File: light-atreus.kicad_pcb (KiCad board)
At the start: 2 copper layers, 40.1 x 44.5 mm, 0 parts

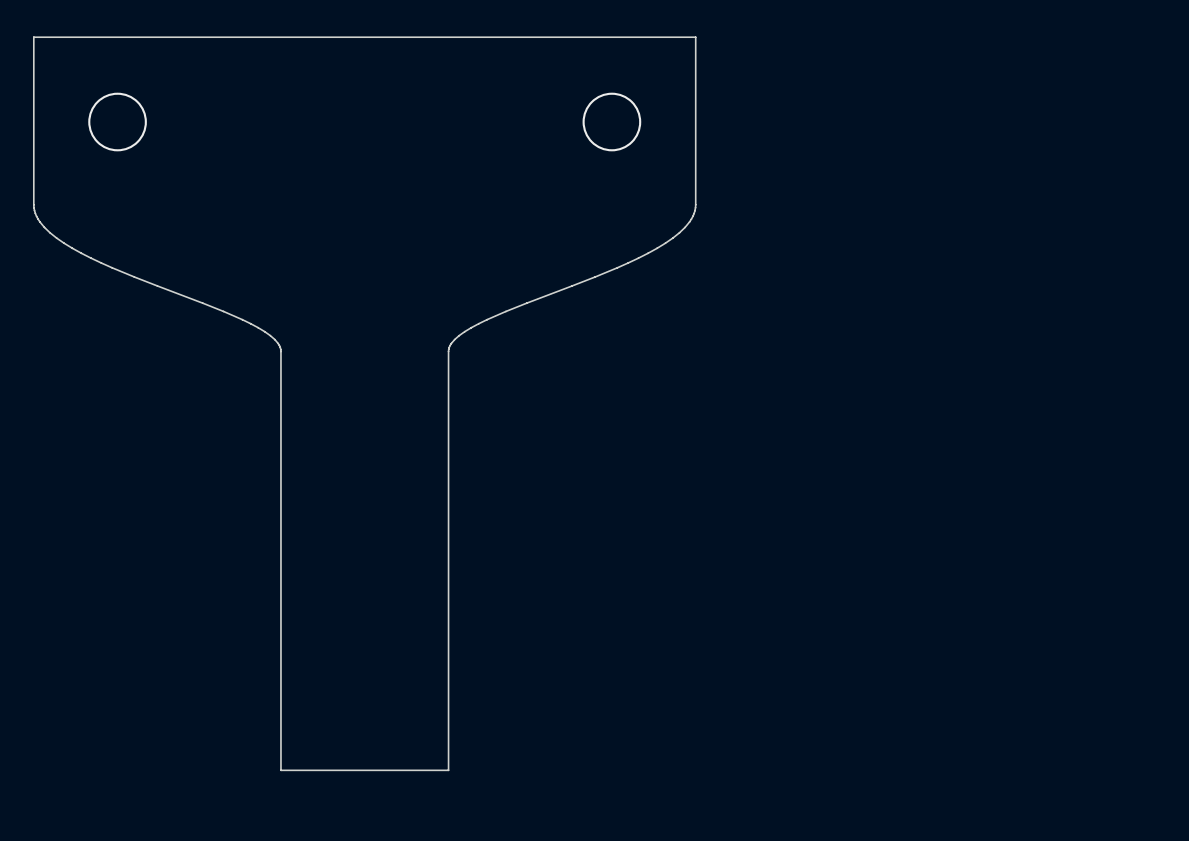
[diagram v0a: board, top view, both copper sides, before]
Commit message: Place USB pads exactly
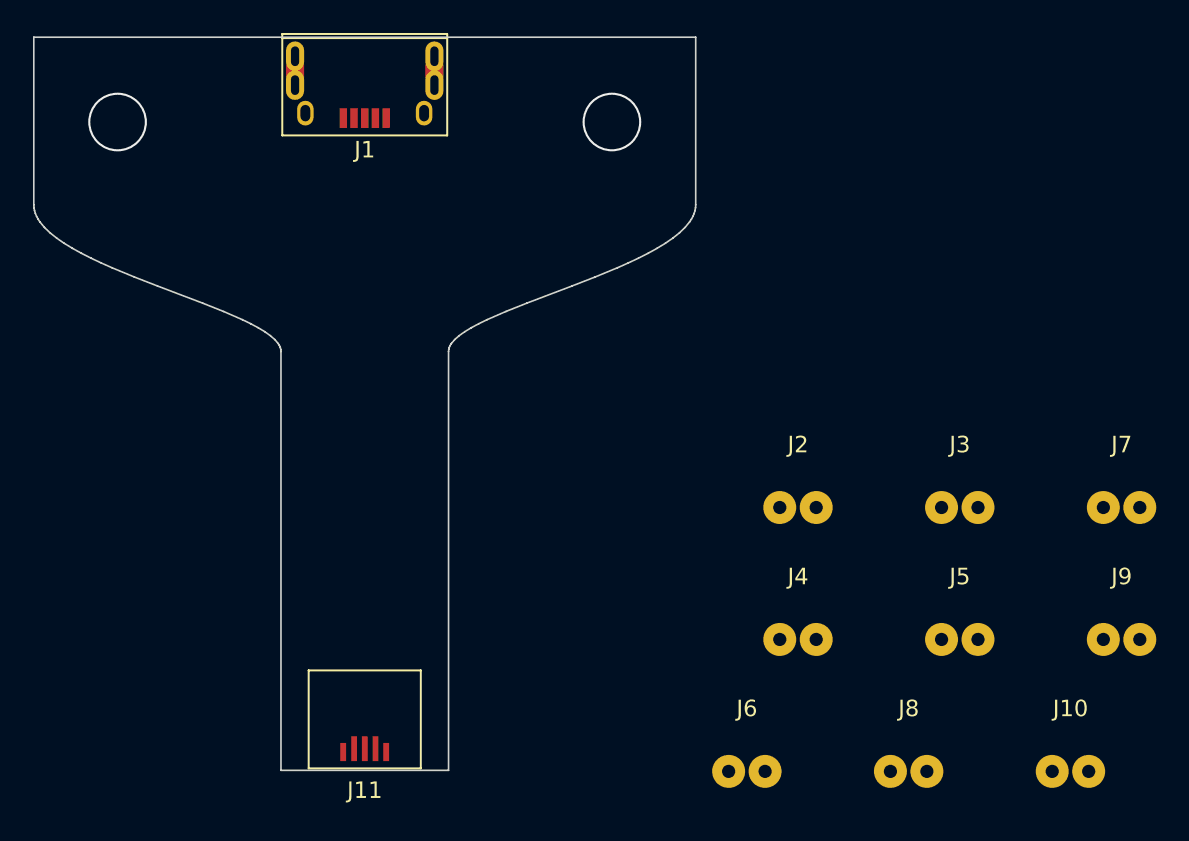
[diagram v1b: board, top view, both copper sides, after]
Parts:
- added J1: USB_B, custom_footprints:USB_Micro-B-custom, F.Cu at (130.3, 75.2)
- added J10: CONN_01X02, custom_footprints:SolderWirePad_1x2-8mm, F.Cu at (173.1, 115.4)
- added J11: USB_B, custom_footprints:USB_Micro-B-custom-plug, F.Cu at (130.3, 114.0)
- added J2: CONN_01X02, custom_footprints:SolderWirePad_1x2-8mm, F.Cu at (156.6, 99.4)
- added J3: CONN_01X02, custom_footprints:SolderWirePad_1x2-8mm, F.Cu at (166.4, 99.4)
- added J4: CONN_01X02, custom_footprints:SolderWirePad_1x2-8mm, F.Cu at (156.6, 107.4)
- added J5: CONN_01X02, custom_footprints:SolderWirePad_1x2-8mm, F.Cu at (166.4, 107.4)
- added J6: CONN_01X02, custom_footprints:SolderWirePad_1x2-8mm, F.Cu at (153.5, 115.4)
- added J7: CONN_01X02, custom_footprints:SolderWirePad_1x2-8mm, F.Cu at (176.2, 99.4)
- added J8: CONN_01X02, custom_footprints:SolderWirePad_1x2-8mm, F.Cu at (163.3, 115.4)
- added J9: CONN_01X02, custom_footprints:SolderWirePad_1x2-8mm, F.Cu at (176.2, 107.4)

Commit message: Locate all wire solder points
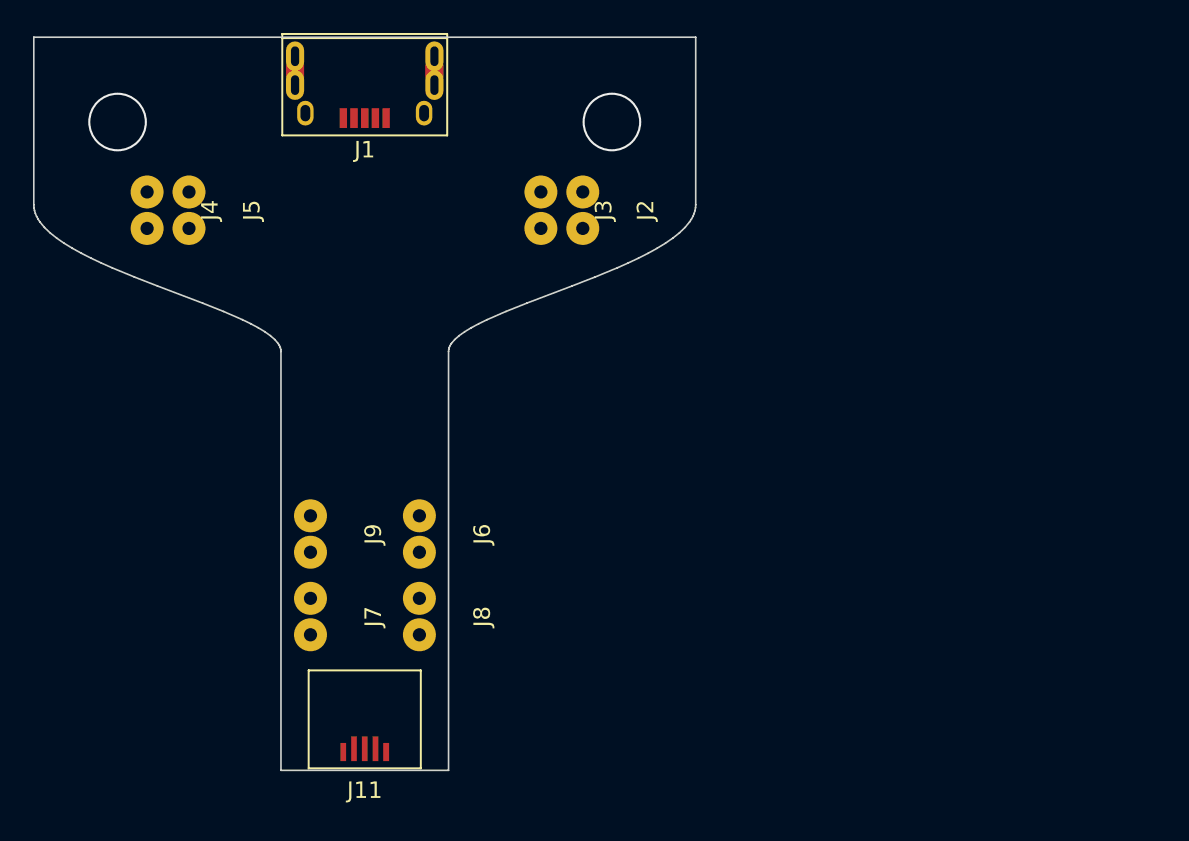
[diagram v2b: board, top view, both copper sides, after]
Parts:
- removed J10: CONN_01X02, custom_footprints:SolderWirePad_1x2-8mm
- moved J5 53.5 mm to (119.6, 81.4), turned to 270 degrees
- moved J7 49.6 mm to (127.0, 106.0), turned to 270 degrees
- moved J9 49.6 mm to (127.0, 101.0), turned to 270 degrees
- moved J4 47.3 mm to (117.1, 81.4), turned to 270 degrees
- moved J3 31.1 mm to (141.0, 81.4), turned to 270 degrees
- moved J8 31.1 mm to (133.6, 106.0), turned to 270 degrees
- moved J6 24.5 mm to (133.6, 101.0), turned to 270 degrees
- moved J2 22.3 mm to (143.5, 81.4), turned to 270 degrees
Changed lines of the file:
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@@
     (tracks 2)
     (zones 0)
-    (modules 11)
-    (nets 15)
+    (modules 10)
+    (nets 14)
   )
   (page A4)
@@
   (net 12 "Net-(J8-Pad2)")
   (net 13 "Net-(J9-Pad2)")
-  (net 14 "Net-(J10-Pad2)")
   (net_class Default "This is the default net class."
     (clearance 0)
@@
     (add_net /SHIELD)
     (add_net /VBUS)
-    (add_net "Net-(J10-Pad2)")
     (add_net "Net-(J2-Pad2)")
     (add_net "Net-(J3-Pad2)")
@@
   )
   (module custom_footprints:SolderWirePad_1x2-8mm (layer F.Cu)
-    (at 156.562257 99.394617)
-    (fp_text reference J2 (at 0 -3.81) (layer F.SilkS)
-      (effects (font (size 1 1) (thickness 0.15)))
-    )
-    (fp_text value CONN_01X02 (at 0.635 2.54) (layer F.Fab)
-      (effects (font (size 1 1) (thickness 0.15)))
-    )
-    (pad 2 thru_hole circle (at 1.1 0) (size 1.99898 1.99898) (drill 0.8001) (layers *.Cu *.Mask)
+    (at 143.51 81.374 270)
+    (fp_text reference J2 (at 0 -3.81 270) (layer F.SilkS)
+      (effects (font (size 1 1) (thickness 0.15)))
+    )
+    (fp_text value CONN_01X02 (at 0.635 2.54 270) (layer F.Fab)
+      (effects (font (size 1 1) (thickness 0.15)))
+    )
+    (pad 2 thru_hole circle (at 1.1 0 270) (size 1.99898 1.99898) (drill 0.8001) (layers *.Cu *.Mask)
       (net 6 "Net-(J2-Pad2)"))
-    (pad 1 thru_hole circle (at -1.11 0) (size 1.99898 1.99898) (drill 0.8001) (layers *.Cu *.Mask)
-      (net 5 /VBUS))
-  )
-  (module custom_footprints:SolderWirePad_1x2-8mm (layer F.Cu)
-    (at 166.372257 99.394617)
-    (fp_text reference J3 (at 0 -3.81) (layer F.SilkS)
-      (effects (font (size 1 1) (thickness 0.15)))
-    )
-    (fp_text value CONN_01X02 (at 0.635 2.54) (layer F.Fab)
-      (effects (font (size 1 1) (thickness 0.15)))
-    )
-    (pad 1 thru_hole circle (at -1.11 0) (size 1.99898 1.99898) (drill 0.8001) (layers *.Cu *.Mask)
-      (net 2 /GND))
-    (pad 2 thru_hole circle (at 1.1 0) (size 1.99898 1.99898) (drill 0.8001) (layers *.Cu *.Mask)
+    (pad 1 thru_hole circle (at -1.11 0 270) (size 1.99898 1.99898) (drill 0.8001) (layers *.Cu *.Mask)
+      (net 5 /VBUS))
+  )
+  (module custom_footprints:SolderWirePad_1x2-8mm (layer F.Cu)
+    (at 140.97 81.374 270)
+    (fp_text reference J3 (at 0 -3.81 270) (layer F.SilkS)
+      (effects (font (size 1 1) (thickness 0.15)))
+    )
+    (fp_text value CONN_01X02 (at 0.635 2.54 270) (layer F.Fab)
+      (effects (font (size 1 1) (thickness 0.15)))
+    )
+    (pad 1 thru_hole circle (at -1.11 0 270) (size 1.99898 1.99898) (drill 0.8001) (layers *.Cu *.Mask)
+      (net 2 /GND))
+    (pad 2 thru_hole circle (at 1.1 0 270) (size 1.99898 1.99898) (drill 0.8001) (layers *.Cu *.Mask)
       (net 7 "Net-(J3-Pad2)"))
   )
   (module custom_footprints:SolderWirePad_1x2-8mm (layer F.Cu)
-    (at 156.562257 107.394617)
-    (fp_text reference J4 (at 0 -3.81) (layer F.SilkS)
-      (effects (font (size 1 1) (thickness 0.15)))
-    )
-    (fp_text value CONN_01X02 (at 0.635 2.54) (layer F.Fab)
-      (effects (font (size 1 1) (thickness 0.15)))
-    )
-    (pad 2 thru_hole circle (at 1.1 0) (size 1.99898 1.99898) (drill 0.8001) (layers *.Cu *.Mask)
+    (at 117.094 81.374 270)
+    (fp_text reference J4 (at 0 -3.81 270) (layer F.SilkS)
+      (effects (font (size 1 1) (thickness 0.15)))
+    )
+    (fp_text value CONN_01X02 (at 0.635 2.54 270) (layer F.Fab)
+      (effects (font (size 1 1) (thickness 0.15)))
+    )
+    (pad 2 thru_hole circle (at 1.1 0 270) (size 1.99898 1.99898) (drill 0.8001) (layers *.Cu *.Mask)
       (net 8 "Net-(J4-Pad2)"))
-    (pad 1 thru_hole circle (at -1.11 0) (size 1.99898 1.99898) (drill 0.8001) (layers *.Cu *.Mask)
-      (net 5 /VBUS))
-  )
-  (module custom_footprints:SolderWirePad_1x2-8mm (layer F.Cu)
-    (at 166.372257 107.394617)
-    (fp_text reference J5 (at 0 -3.81) (layer F.SilkS)
-      (effects (font (size 1 1) (thickness 0.15)))
-    )
-    (fp_text value CONN_01X02 (at 0.635 2.54) (layer F.Fab)
-      (effects (font (size 1 1) (thickness 0.15)))
-    )
-    (pad 1 thru_hole circle (at -1.11 0) (size 1.99898 1.99898) (drill 0.8001) (layers *.Cu *.Mask)
-      (net 2 /GND))
-    (pad 2 thru_hole circle (at 1.1 0) (size 1.99898 1.99898) (drill 0.8001) (layers *.Cu *.Mask)
+    (pad 1 thru_hole circle (at -1.11 0 270) (size 1.99898 1.99898) (drill 0.8001) (layers *.Cu *.Mask)
+      (net 5 /VBUS))
+  )
+  (module custom_footprints:SolderWirePad_1x2-8mm (layer F.Cu)
+    (at 119.634 81.374 270)
+    (fp_text reference J5 (at 0 -3.81 270) (layer F.SilkS)
+      (effects (font (size 1 1) (thickness 0.15)))
+    )
+    (fp_text value CONN_01X02 (at 0.635 2.54 270) (layer F.Fab)
+      (effects (font (size 1 1) (thickness 0.15)))
+    )
+    (pad 1 thru_hole circle (at -1.11 0 270) (size 1.99898 1.99898) (drill 0.8001) (layers *.Cu *.Mask)
+      (net 2 /GND))
+    (pad 2 thru_hole circle (at 1.1 0 270) (size 1.99898 1.99898) (drill 0.8001) (layers *.Cu *.Mask)
       (net 9 "Net-(J5-Pad2)"))
   )
   (module custom_footprints:SolderWirePad_1x2-8mm (layer F.Cu)
-    (at 153.462257 115.394617)
-    (fp_text reference J6 (at 0 -3.81) (layer F.SilkS)
-      (effects (font (size 1 1) (thickness 0.15)))
-    )
-    (fp_text value CONN_01X02 (at 0.635 2.54) (layer F.Fab)
-      (effects (font (size 1 1) (thickness 0.15)))
-    )
-    (pad 2 thru_hole circle (at 1.1 0) (size 1.99898 1.99898) (drill 0.8001) (layers *.Cu *.Mask)
+    (at 133.604 101.008 270)
+    (fp_text reference J6 (at 0 -3.81 270) (layer F.SilkS)
+      (effects (font (size 1 1) (thickness 0.15)))
+    )
+    (fp_text value CONN_01X02 (at 0.635 2.54 270) (layer F.Fab)
+      (effects (font (size 1 1) (thickness 0.15)))
+    )
+    (pad 2 thru_hole circle (at 1.1 0 270) (size 1.99898 1.99898) (drill 0.8001) (layers *.Cu *.Mask)
       (net 10 "Net-(J6-Pad2)"))
-    (pad 1 thru_hole circle (at -1.11 0) (size 1.99898 1.99898) (drill 0.8001) (layers *.Cu *.Mask)
-      (net 5 /VBUS))
-  )
-  (module custom_footprints:SolderWirePad_1x2-8mm (layer F.Cu)
-    (at 176.182257 99.394617)
-    (fp_text reference J7 (at 0 -3.81) (layer F.SilkS)
-      (effects (font (size 1 1) (thickness 0.15)))
-    )
-    (fp_text value CONN_01X02 (at 0.635 2.54) (layer F.Fab)
-      (effects (font (size 1 1) (thickness 0.15)))
-    )
-    (pad 1 thru_hole circle (at -1.11 0) (size 1.99898 1.99898) (drill 0.8001) (layers *.Cu *.Mask)
+    (pad 1 thru_hole circle (at -1.11 0 270) (size 1.99898 1.99898) (drill 0.8001) (layers *.Cu *.Mask)
+      (net 5 /VBUS))
+  )
+  (module custom_footprints:SolderWirePad_1x2-8mm (layer F.Cu)
+    (at 127 106.012 270)
+    (fp_text reference J7 (at 0 -3.81 270) (layer F.SilkS)
+      (effects (font (size 1 1) (thickness 0.15)))
+    )
+    (fp_text value CONN_01X02 (at 0.635 2.54 270) (layer F.Fab)
+      (effects (font (size 1 1) (thickness 0.15)))
+    )
+    (pad 1 thru_hole circle (at -1.11 0 270) (size 1.99898 1.99898) (drill 0.8001) (layers *.Cu *.Mask)
       (net 3 /D+))
-    (pad 2 thru_hole circle (at 1.1 0) (size 1.99898 1.99898) (drill 0.8001) (layers *.Cu *.Mask)
+    (pad 2 thru_hole circle (at 1.1 0 270) (size 1.99898 1.99898) (drill 0.8001) (layers *.Cu *.Mask)
       (net 11 "Net-(J7-Pad2)"))
   )
   (module custom_footprints:SolderWirePad_1x2-8mm (layer F.Cu)
-    (at 163.272257 115.394617)
-    (fp_text reference J8 (at 0 -3.81) (layer F.SilkS)
-      (effects (font (size 1 1) (thickness 0.15)))
-    )
-    (fp_text value CONN_01X02 (at 0.635 2.54) (layer F.Fab)
-      (effects (font (size 1 1) (thickness 0.15)))
-    )
-    (pad 2 thru_hole circle (at 1.1 0) (size 1.99898 1.99898) (drill 0.8001) (layers *.Cu *.Mask)
+    (at 133.604 106.012 270)
+    (fp_text reference J8 (at 0 -3.81 270) (layer F.SilkS)
+      (effects (font (size 1 1) (thickness 0.15)))
+    )
+    (fp_text value CONN_01X02 (at 0.635 2.54 270) (layer F.Fab)
+      (effects (font (size 1 1) (thickness 0.15)))
+    )
+    (pad 2 thru_hole circle (at 1.1 0 270) (size 1.99898 1.99898) (drill 0.8001) (layers *.Cu *.Mask)
       (net 12 "Net-(J8-Pad2)"))
-    (pad 1 thru_hole circle (at -1.11 0) (size 1.99898 1.99898) (drill 0.8001) (layers *.Cu *.Mask)
+    (pad 1 thru_hole circle (at -1.11 0 270) (size 1.99898 1.99898) (drill 0.8001) (layers *.Cu *.Mask)
       (net 4 /D-))
   )
   (module custom_footprints:SolderWirePad_1x2-8mm (layer F.Cu)
-    (at 176.182257 107.394617)
-    (fp_text reference J9 (at 0 -3.81) (layer F.SilkS)
-      (effects (font (size 1 1) (thickness 0.15)))
-    )
-    (fp_text value CONN_01X02 (at 0.635 2.54) (layer F.Fab)
-      (effects (font (size 1 1) (thickness 0.15)))
-    )
-    (pad 2 thru_hole circle (at 1.1 0) (size 1.99898 1.99898) (drill 0.8001) (layers *.Cu *.Mask)
+    (at 127 101.008 270)
+    (fp_text reference J9 (at 0 -3.81 270) (layer F.SilkS)
+      (effects (font (size 1 1) (thickness 0.15)))
+    )
+    (fp_text value CONN_01X02 (at 0.635 2.54 270) (layer F.Fab)
+      (effects (font (size 1 1) (thickness 0.15)))
+    )
+    (pad 2 thru_hole circle (at 1.1 0 270) (size 1.99898 1.99898) (drill 0.8001) (layers *.Cu *.Mask)
       (net 13 "Net-(J9-Pad2)"))
-    (pad 1 thru_hole circle (at -1.11 0) (size 1.99898 1.99898) (drill 0.8001) (layers *.Cu *.Mask)
-      (net 2 /GND))
-  )
-  (module custom_footprints:SolderWirePad_1x2-8mm (layer F.Cu)
-    (at 173.082257 115.394617)
-    (fp_text reference J10 (at 0 -3.81) (layer F.SilkS)
-      (effects (font (size 1 1) (thickness 0.15)))
-    )
-    (fp_text value CONN_01X02 (at 0.635 2.54) (layer F.Fab)
-      (effects (font (size 1 1) (thickness 0.15)))
-    )
-    (pad 1 thru_hole circle (at -1.11 0) (size 1.99898 1.99898) (drill 0.8001) (layers *.Cu *.Mask)
-      (net 1 /SHIELD))
-    (pad 2 thru_hole circle (at 1.1 0) (size 1.99898 1.99898) (drill 0.8001) (layers *.Cu *.Mask)
-      (net 14 "Net-(J10-Pad2)"))
+    (pad 1 thru_hole circle (at -1.11 0 270) (size 1.99898 1.99898) (drill 0.8001) (layers *.Cu *.Mask)
+      (net 2 /GND))
   )
   (module custom_footprints:USB_Micro-B-custom-plug locked (layer F.Cu)
